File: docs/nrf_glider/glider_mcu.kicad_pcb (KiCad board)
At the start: 2 copper layers, 8 parts, among them J1 PROG, J2 Conn_01x06_Male, J3 Conn_01x06_Male, U1 MSP430G2553IPW20, U2 25LC640, U3 NRF24L01_Breakout

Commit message: Version 2 routing PDF
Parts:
- added REF**: MountingHole_3.2mm_M3, MountingHole:MountingHole_3.2mm_M3, F.Cu at (26.7, 25.4)
- added REF**: MountingHole_3.2mm_M3, MountingHole:MountingHole_3.2mm_M3, F.Cu at (69.8, 77.5)
- added REF**: MountingHole_3.2mm_M3, MountingHole:MountingHole_3.2mm_M3, F.Cu at (26.7, 77.5)
- moved J1 113.2 mm to (41.9, 77.5)
- moved U1 111.9 mm to (44.5, 43.2)
- moved U2 111.9 mm to (66.0, 49.5)
- moved J2 111.9 mm to (27.9, 47.0)
- moved J3 111.9 mm to (71.1, 47.0)
- moved R1 111.9 mm to (33.0, 41.9)
- moved R2 111.9 mm to (33.0, 68.6)
- moved U3 111.9 mm to (63.5, 34.3)
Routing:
- net Net-(U1-Pad7): track 69.5 -> 92.0 mm
- net Net-(U1-Pad19): track 27.5 -> 46.3 mm
- net GND: track 99.6 -> 112.2 mm
- net Net-(U1-Pad14): track 45.2 -> 49.2 mm
- net Net-(U1-Pad18): track 32.8 -> 29.3 mm
- net Net-(J1-Pad3): track 60.5 -> 57.7 mm
- net Net-(J1-Pad2): track 62.9 -> 60.1 mm
- net Net-(J3-Pad3): track 46.5 -> 44.0 mm
- net VCC: track 110.7 -> 112.9 mm
- net Net-(J3-Pad1): track 26.6 -> 28.4 mm
- net Net-(J1-Pad5): track 28.2 -> 27.0 mm
- net Net-(U1-Pad15): track 36.2 -> 35.4 mm
- net Net-(J3-Pad4): track 52.3 -> 51.6 mm
- net Net-(J3-Pad5): track 57.4 -> 56.7 mm
- net Net-(U1-Pad13): track 41.5 -> 40.9 mm
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- added copper zone on F.Cu, net GND
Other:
- net class Default: via_dia 0.8 -> 1.4; via_drill 0.4 -> 0.6
- board text added: "H4H NRF Glider"
- board text added: "v 0.9"

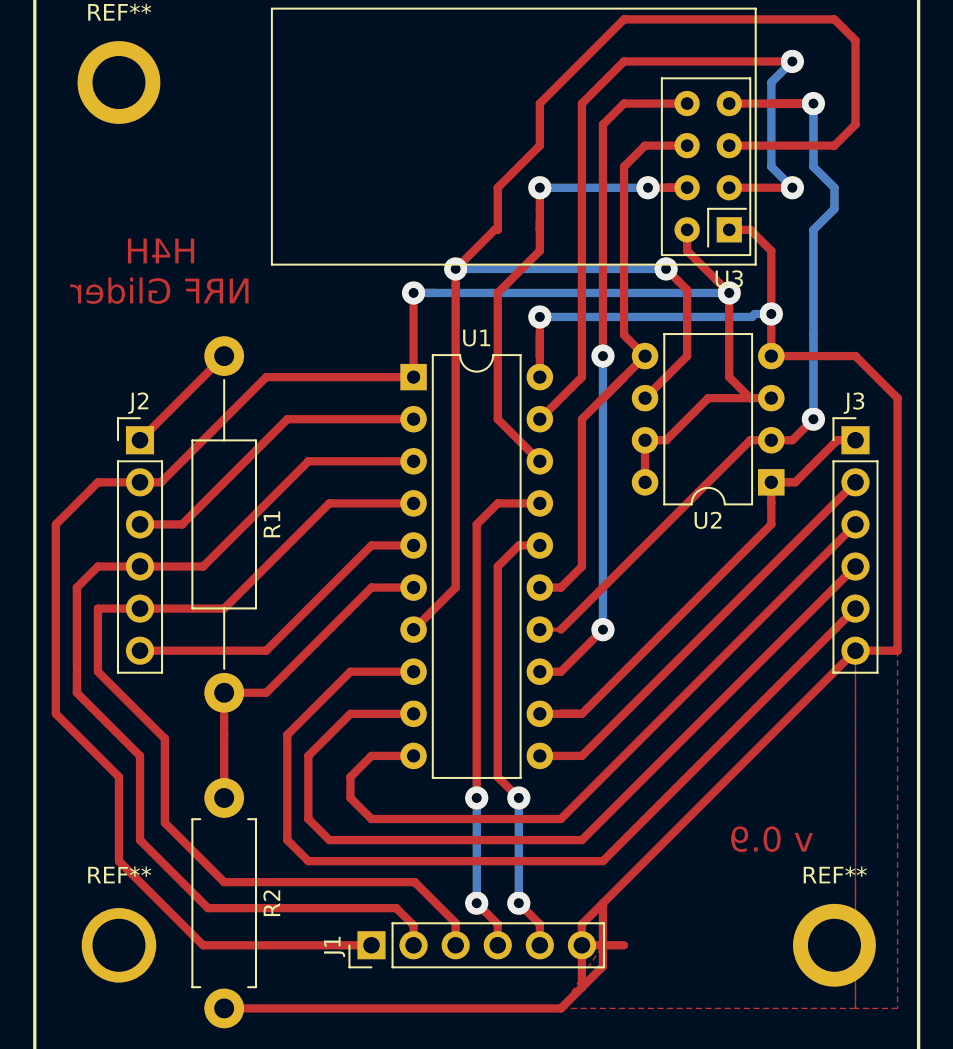
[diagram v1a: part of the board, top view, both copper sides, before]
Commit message: Rerouted Rx module for center buzzer
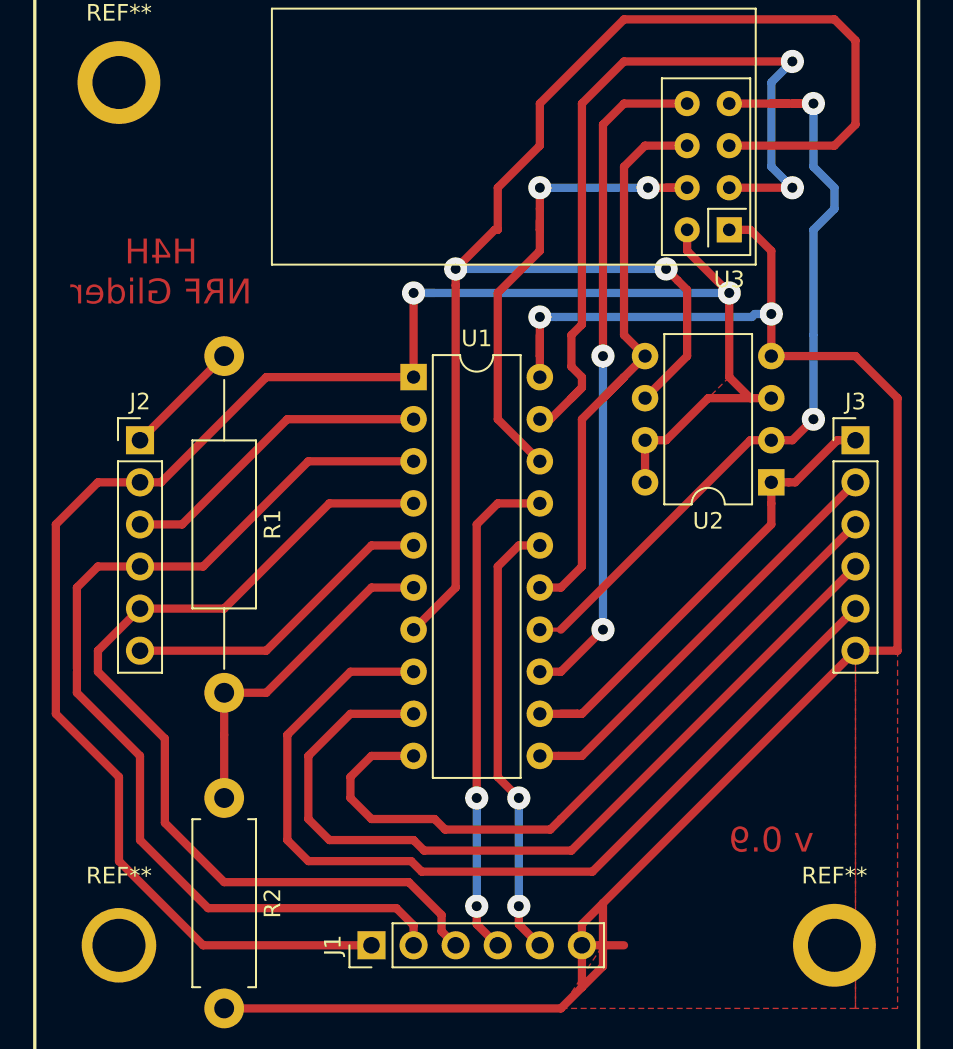
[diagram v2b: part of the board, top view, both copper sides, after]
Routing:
- net Net-(U1-Pad19): track 46.3 -> 48.1 mm
- net Net-(J1-Pad3): track 57.7 -> 56.0 mm
- net Net-(J3-Pad3): track 44.0 -> 44.5 mm
- net Net-(J3-Pad5): track 56.7 -> 57.2 mm
- net Net-(J3-Pad4): track 51.6 -> 52.1 mm
- added copper zone on F.Cu, net VCC
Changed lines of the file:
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@@
     (thickness 1.6)
     (drawings 6)
-    (tracks 246)
+    (tracks 257)
     (zones 0)
     (modules 11)
@@
       (padsonsilk false)
       (subtractmaskfromsilk false)
-      (outputformat 4)
+      (outputformat 2)
       (mirror true)
       (drillshape 1)
@@
   (segment (start 33.02 57.15) (end 27.94 57.15) (width 0.5) (layer F.Cu) (net 3))
   (segment (start 33.02 57.15) (end 39.37 50.8) (width 0.5) (layer F.Cu) (net 3))
-  (segment (start 46.99 76.123692) (end 46.99 77.47) (width 0.5) (layer F.Cu) (net 3))
-  (segment (start 44.526308 73.66) (end 46.99 76.123692) (width 0.5) (layer F.Cu) (net 3))
-  (segment (start 25.4 57.15) (end 25.4 60.96) (width 0.5) (layer F.Cu) (net 3))
-  (segment (start 27.94 57.15) (end 25.4 57.15) (width 0.5) (layer F.Cu) (net 3))
-  (segment (start 25.4 60.96) (end 29.440022 65.000022) (width 0.5) (layer F.Cu) (net 3))
   (segment (start 29.440022 65.000022) (end 29.440022 70.080022) (width 0.5) (layer F.Cu) (net 3))
   (segment (start 29.440022 70.080022) (end 33.02 73.66) (width 0.5) (layer F.Cu) (net 3))
-  (segment (start 33.02 73.66) (end 44.526308 73.66) (width 0.5) (layer F.Cu) (net 3))
+  (segment (start 33.02 73.66) (end 44.161542 73.66) (width 0.5) (layer F.Cu) (net 3))
+  (segment (start 44.161542 73.66) (end 46.140001 75.638459) (width 0.5) (layer F.Cu) (net 3))
+  (segment (start 25.4 60.96) (end 29.440022 65.000022) (width 0.5) (layer F.Cu) (net 3))
+  (segment (start 46.140001 76.620001) (end 46.99 77.47) (width 0.5) (layer F.Cu) (net 3))
+  (segment (start 46.140001 75.638459) (end 46.140001 76.620001) (width 0.5) (layer F.Cu) (net 3))
+  (segment (start 25.4 59.69) (end 25.4 60.96) (width 0.5) (layer F.Cu) (net 3))
+  (segment (start 27.94 57.15) (end 25.4 59.69) (width 0.5) (layer F.Cu) (net 3))
   (segment (start 52.07 50.8) (end 49.53 50.8) (width 0.5) (layer F.Cu) (net 4))
   (segment (start 49.53 50.8) (end 48.26 52.07) (width 0.5) (layer F.Cu) (net 4))
@@
   (segment (start 48.26 68.58) (end 48.26 68.58) (width 0.5) (layer F.Cu) (net 4))
   (via (at 48.26 68.58) (size 1.4) (drill 0.6) (layers F.Cu B.Cu) (net 4))
-  (via (at 48.26 74.93) (size 1.4) (drill 0.6) (layers F.Cu B.Cu) (net 4))
-  (segment (start 49.53 77.47) (end 49.53 76.2) (width 0.5) (layer F.Cu) (net 4))
-  (segment (start 49.53 76.2) (end 48.26 74.93) (width 0.5) (layer F.Cu) (net 4))
-  (segment (start 48.26 74.93) (end 48.26 68.58) (width 0.5) (layer B.Cu) (net 4))
+  (segment (start 48.26 76.2) (end 48.26 76.099959) (width 0.5) (layer F.Cu) (net 4))
+  (segment (start 48.26 68.58) (end 48.26 75.11001) (width 0.5) (layer B.Cu) (net 4))
+  (segment (start 49.53 77.47) (end 48.26 76.2) (width 0.5) (layer F.Cu) (net 4))
+  (via (at 48.26 75.11001) (size 1.4) (drill 0.6) (layers F.Cu B.Cu) (net 4))
+  (segment (start 48.26 76.099959) (end 48.26 75.11001) (width 0.5) (layer F.Cu) (net 4))
   (segment (start 50.8 68.58) (end 50.8 68.58) (width 0.5) (layer F.Cu) (net 5))
   (segment (start 50.8 53.34) (end 49.53 54.61) (width 0.5) (layer F.Cu) (net 5))
@@
   (segment (start 50.8 68.58) (end 50.8 68.58) (width 0.5) (layer F.Cu) (net 5))
   (via (at 50.8 68.58) (size 1.4) (drill 0.6) (layers F.Cu B.Cu) (net 5))
-  (via (at 50.8 74.93) (size 1.4) (drill 0.6) (layers F.Cu B.Cu) (net 5))
-  (segment (start 52.07 77.47) (end 52.07 76.2) (width 0.5) (layer F.Cu) (net 5))
-  (segment (start 52.07 76.2) (end 50.8 74.93) (width 0.5) (layer F.Cu) (net 5))
-  (segment (start 50.8 68.58) (end 50.8 74.93) (width 0.5) (layer B.Cu) (net 5))
+  (segment (start 50.8 68.58) (end 50.8 75.11001) (width 0.5) (layer B.Cu) (net 5))
+  (segment (start 50.8 76.2) (end 50.8 76.099959) (width 0.5) (layer F.Cu) (net 5))
+  (segment (start 50.8 76.099959) (end 50.8 75.11001) (width 0.5) (layer F.Cu) (net 5))
+  (segment (start 52.07 77.47) (end 50.8 76.2) (width 0.5) (layer F.Cu) (net 5))
+  (via (at 50.8 75.11001) (size 1.4) (drill 0.6) (layers F.Cu B.Cu) (net 5))
   (segment (start 71.12 59.69) (end 73.66 59.69) (width 0.5) (layer F.Cu) (net 6))
   (segment (start 73.66 59.69) (end 73.66 44.45) (width 0.5) (layer F.Cu) (net 6))
@@
   (segment (start 45.72 69.85) (end 45.72 69.85) (width 0.5) (layer F.Cu) (net 12))
   (segment (start 53.34 69.85) (end 53.34 69.85) (width 0.5) (layer F.Cu) (net 12))
-  (segment (start 41.91 69.85) (end 53.34 69.85) (width 0.5) (layer F.Cu) (net 12))
   (segment (start 40.64 67.31) (end 40.64 68.58) (width 0.5) (layer F.Cu) (net 12))
   (segment (start 41.91 66.04) (end 40.64 67.31) (width 0.5) (layer F.Cu) (net 12))
@@
   (segment (start 40.64 68.58) (end 41.91 69.85) (width 0.5) (layer F.Cu) (net 12))
   (segment (start 44.45 66.04) (end 41.91 66.04) (width 0.5) (layer F.Cu) (net 12))
-  (segment (start 45.72 71.12) (end 45.72 71.12) (width 0.5) (layer F.Cu) (net 13))
-  (segment (start 53.34 71.12) (end 53.34 71.12) (width 0.5) (layer F.Cu) (net 13))
-  (segment (start 39.37 71.12) (end 54.61 71.12) (width 0.5) (layer F.Cu) (net 13))
-  (segment (start 38.1 69.85) (end 39.37 71.12) (width 0.5) (layer F.Cu) (net 13))
-  (segment (start 38.1 66.04) (end 38.1 69.85) (width 0.5) (layer F.Cu) (net 13))
-  (segment (start 40.64 63.5) (end 38.1 66.04) (width 0.5) (layer F.Cu) (net 13))
-  (segment (start 54.61 71.12) (end 71.12 54.61) (width 0.5) (layer F.Cu) (net 13))
-  (segment (start 44.45 63.5) (end 40.64 63.5) (width 0.5) (layer F.Cu) (net 13))
-  (segment (start 45.72 72.39) (end 45.72 72.39) (width 0.5) (layer F.Cu) (net 14))
-  (segment (start 53.34 72.39) (end 53.34 72.39) (width 0.5) (layer F.Cu) (net 14))
+  (segment (start 41.91 69.85) (end 45.72 69.85) (width 0.5) (layer F.Cu) (net 12))
+  (segment (start 46.355 70.485) (end 52.705 70.485) (width 0.5) (layer F.Cu) (net 12))
+  (segment (start 52.705 70.485) (end 53.34 69.85) (width 0.5) (layer F.Cu) (net 12))
+  (segment (start 45.72 69.85) (end 46.355 70.485) (width 0.5) (layer F.Cu) (net 12))
+  (segment (start 38.1 66.04) (end 40.64 63.5) (width 0.5) (layer F.Cu) (net 13))
+  (segment (start 40.64 63.5) (end 44.45 63.5) (width 0.5) (layer F.Cu) (net 13))
+  (segment (start 44.45 71.12) (end 39.37 71.12) (width 0.5) (layer F.Cu) (net 13))
+  (segment (start 39.37 71.12) (end 38.1 69.85) (width 0.5) (layer F.Cu) (net 13))
+  (segment (start 38.1 69.85) (end 38.1 66.04) (width 0.5) (layer F.Cu) (net 13))
+  (segment (start 45.085 71.755) (end 53.975 71.755) (width 0.5) (layer F.Cu) (net 13))
+  (segment (start 71.12 54.61) (end 53.975 71.755) (width 0.5) (layer F.Cu) (net 13))
+  (segment (start 45.085 71.755) (end 44.45 71.12) (width 0.5) (layer F.Cu) (net 13))
+  (segment (start 44.940771 73.025) (end 55.245 73.025) (width 0.5) (layer F.Cu) (net 14))
   (segment (start 44.45 60.96) (end 40.64 60.96) (width 0.5) (layer F.Cu) (net 14))
-  (segment (start 55.88 72.39) (end 69.944999 58.325001) (width 0.5) (layer F.Cu) (net 14))
-  (segment (start 69.944999 58.325001) (end 71.12 57.15) (width 0.5) (layer F.Cu) (net 14))
   (segment (start 40.64 60.96) (end 36.83 64.77) (width 0.5) (layer F.Cu) (net 14))
+  (segment (start 44.305771 72.39) (end 44.940771 73.025) (width 0.5) (layer F.Cu) (net 14))
+  (segment (start 55.245 73.025) (end 71.12 57.15) (width 0.5) (layer F.Cu) (net 14))
   (segment (start 36.83 64.77) (end 36.83 71.12) (width 0.5) (layer F.Cu) (net 14))
   (segment (start 36.83 71.12) (end 38.1 72.39) (width 0.5) (layer F.Cu) (net 14))
-  (segment (start 38.1 72.39) (end 55.88 72.39) (width 0.5) (layer F.Cu) (net 14))
+  (segment (start 38.1 72.39) (end 44.305771 72.39) (width 0.5) (layer F.Cu) (net 14))
   (segment (start 44.45 55.88) (end 41.91 55.88) (width 0.5) (layer F.Cu) (net 15))
   (segment (start 33.02 64.77) (end 33.02 68.58) (width 0.5) (layer F.Cu) (net 15))
@@
   (segment (start 67.31 31.75) (end 67.31 31.75) (width 0.5) (layer F.Cu) (net 21))
   (segment (start 57.15 24.13) (end 67.31 24.13) (width 0.5) (layer F.Cu) (net 21))
-  (segment (start 52.07 45.72) (end 54.61 43.18) (width 0.5) (layer F.Cu) (net 21))
   (segment (start 54.61 26.67) (end 57.15 24.13) (width 0.5) (layer F.Cu) (net 21))
-  (segment (start 54.61 43.18) (end 54.61 26.67) (width 0.5) (layer F.Cu) (net 21))
   (segment (start 67.31 31.75) (end 67.31 31.75) (width 0.5) (layer F.Cu) (net 21))
   (via (at 67.31 31.75) (size 1.4) (drill 0.6) (layers F.Cu B.Cu) (net 21))
@@
   (segment (start 66.04 25.4) (end 66.04 30.48) (width 0.5) (layer B.Cu) (net 21))
   (segment (start 66.04 30.48) (end 67.31 31.75) (width 0.5) (layer B.Cu) (net 21))
+  (segment (start 54.61 40.005) (end 53.975 40.64) (width 0.5) (layer F.Cu) (net 21))
+  (segment (start 54.61 40.005) (end 54.61 26.67) (width 0.5) (layer F.Cu) (net 21))
+  (segment (start 53.975 40.64) (end 53.975 42.545) (width 0.5) (layer F.Cu) (net 21))
+  (segment (start 53.975 42.545) (end 54.61 43.18) (width 0.5) (layer F.Cu) (net 21))
+  (segment (start 54.61 43.18) (end 54.61 43.815) (width 0.5) (layer F.Cu) (net 21))
+  (segment (start 54.61 43.815) (end 53.975 44.45) (width 0.5) (layer F.Cu) (net 21))
+  (segment (start 52.07 45.72) (end 52.705 45.72) (width 0.5) (layer F.Cu) (net 21))
+  (segment (start 52.705 45.72) (end 54.61 43.815) (width 0.5) (layer F.Cu) (net 21))
   (zone (net 6) (net_name GND) (layer F.Cu) (hatch edge 0.508)
     (connect_pads (clearance 0.508))
@@
       )
     )
+  )
+  (zone (net 1) (net_name VCC) (layer F.Cu) (hatch edge 0.508)
+    (connect_pads (clearance 0.508))
+    (min_thickness 0.254)
+    (fill yes (arc_segments 16) (thermal_gap 0.508) (thermal_bridge_width 0.508))
+    (polygon
+      (pts
+        (xy 64.77 44.45) (xy 63.5 43.18) (xy 62.23 44.45)
+      )
+    )
